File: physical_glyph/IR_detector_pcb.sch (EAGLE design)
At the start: 37 parts, among them IC1 7805T, IC2 LM339N, U1 MCP6004-I/P

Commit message: Added PCB design
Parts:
- removed IC1: 7805T, linear:7805T
- added C10, C11, C12, C13: 0.1uF, resistor:C-EU025-024X044
- added D2: 1N4004, diode:1N4004
- added J1: (no value), SparkFun-Connectors:CONN_025MM
- added J2: (no value), SparkFun-Connectors:CONN_02
- added Q2: (no value), SparkFun-Sensors:LTR-301
- added R24, R31, R33, R34, R40, R44: 1k, rcl:R-US_0204/2V
- added R25, R30, R32, R38, R41: 10k, rcl:R-US_0204/2V
- added R26, R27, R28, R45, R46: 1M, rcl:R-US_0204/2V
- added R29: 3.9k, rcl:R-US_0204/2V
- added R35, R36, R37, R39: 100k, rcl:R-US_0204/2V
- added R42, R43: 4.7k, rcl:R-US_0204/2V
- added U2: MCP6004-I/P, Microchip_By_element14_Batch_1:MCP6004-I/P
- C2: value 0.1uF -> 10uF
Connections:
- removed net VIN: C1.1, IC1.VI
- new net 2.5V2: R39.1, R40.2, U2.VINC-, U2.VOUTC
- new net COMP_OUT2: IC2A.OUT, R27.1, R29.2, R31.2
- new net GAIN2_IN2: C13.1, R39.2, U2.VIND+
- new net GAIN2_OUT2: C11.2, R42.2, U2.VOUTD
- new net GAIN_OUT2: C13.2, R43.2, U2.VOUTA
- new net IR_SIGNAL2: C10.1, R33.2, U2.VINA+
- new net MICRO_IN2: J2.2, R30.2, R31.1
- new net N$10: C10.2, Q2.E1, R32.1
- new net N$11: D2.A, U2.VOUTB
- new net N$12: C12.1, R36.1, R37.2, U2.VINC+
- new net N$13: R24.1, R38.1, U2.VINA-
- new net N$14: R40.1, R41.1, U2.VIND-
- new net N$15: R41.2, R42.1
- new net N$16: R38.2, R43.1
- new net N$17: R34.1, R44.2
- new net N$9: IC2A.-IN, R26.2, R27.2, R28.2, R45.2, R46.2
- new net PEAK_DIODE2: D2.C, R34.2, U2.VINB-
- new net PEAK_IN2: C11.1, R35.2, U2.VINB+
- new net PEAK_OUT2: C2.2, IC2A.+IN, R25.2, R44.1
- net 5V: now also C1.2, J1.1, Q2.C1, R26.1, R29.1, R36.2, U2.VDD; no longer C2.2, IC1.VO
- net COMP_OUT: now also IC2D.OUT; no longer IC2A.OUT
- net GND: now also C1.1, C12.2, J1.2, R24.2, R25.1, R28.1, R30.1, R32.2, R33.1, R35.1, R37.1, R45.1, R46.1, U2.VSS; no longer C1.2, IC1.GND
- net MICRO_IN: now also J2.1
- net N$34: now also IC2D.-IN; no longer IC2A.-IN
- net PEAK_OUT: now also IC2D.+IN; no longer IC2A.+IN
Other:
- note added: "Output header pins"
- note added: "Power Terminal Block"
- note removed: "Package option used here is TSSOP but I am using DIP"
- moved on the sheet: C1, C2, IC2A

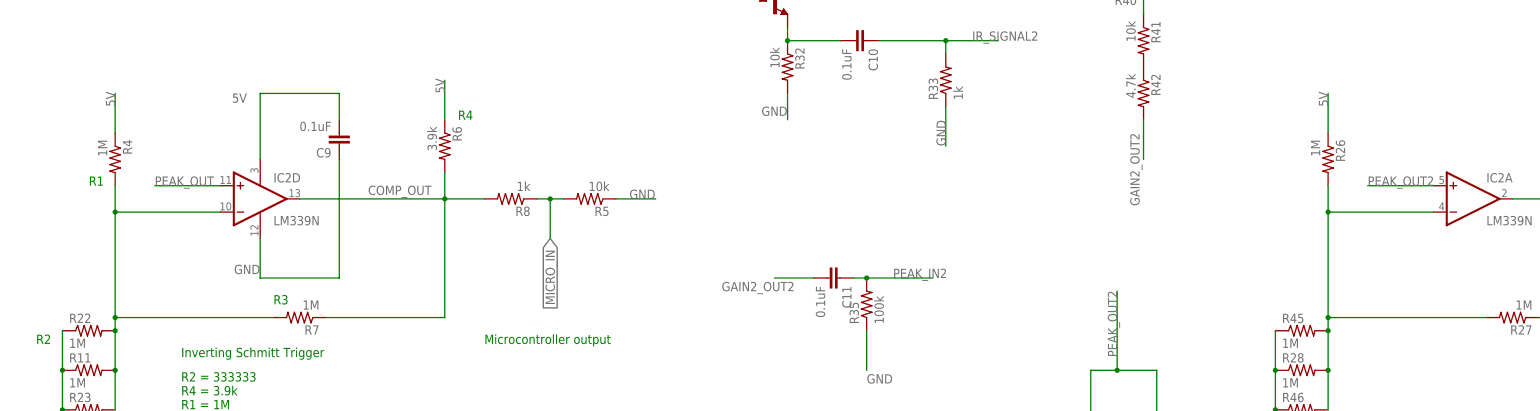
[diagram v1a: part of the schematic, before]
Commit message: Fixed a long standing regression with the IR circuit
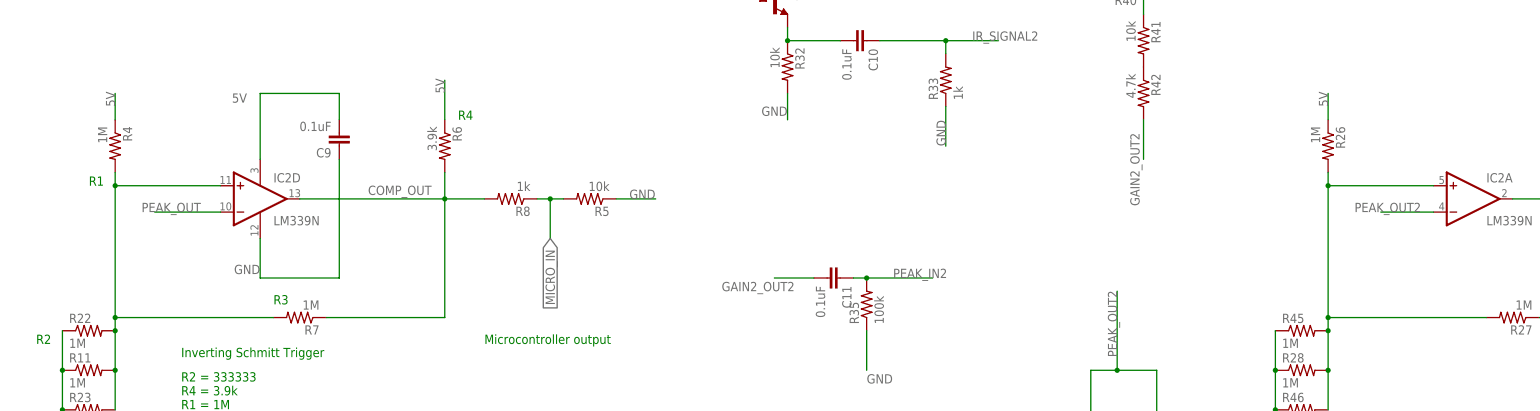
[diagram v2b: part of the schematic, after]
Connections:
- net N$34: now also IC2D.+IN; no longer IC2D.-IN
- net N$9: now also IC2A.+IN; no longer IC2A.-IN
- net PEAK_OUT: now also IC2D.-IN; no longer IC2D.+IN
- net PEAK_OUT2: now also IC2A.-IN; no longer IC2A.+IN
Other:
- moved on the sheet: R26, R4
